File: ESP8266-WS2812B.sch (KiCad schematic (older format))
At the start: 17 parts, among them J1 USB_B_Micro, J2 Alternate_Power_Input, J3 Conn_01x06, J4 Conn_01x03, Q1 Q_NPN_BEC, SW1 SW_Push

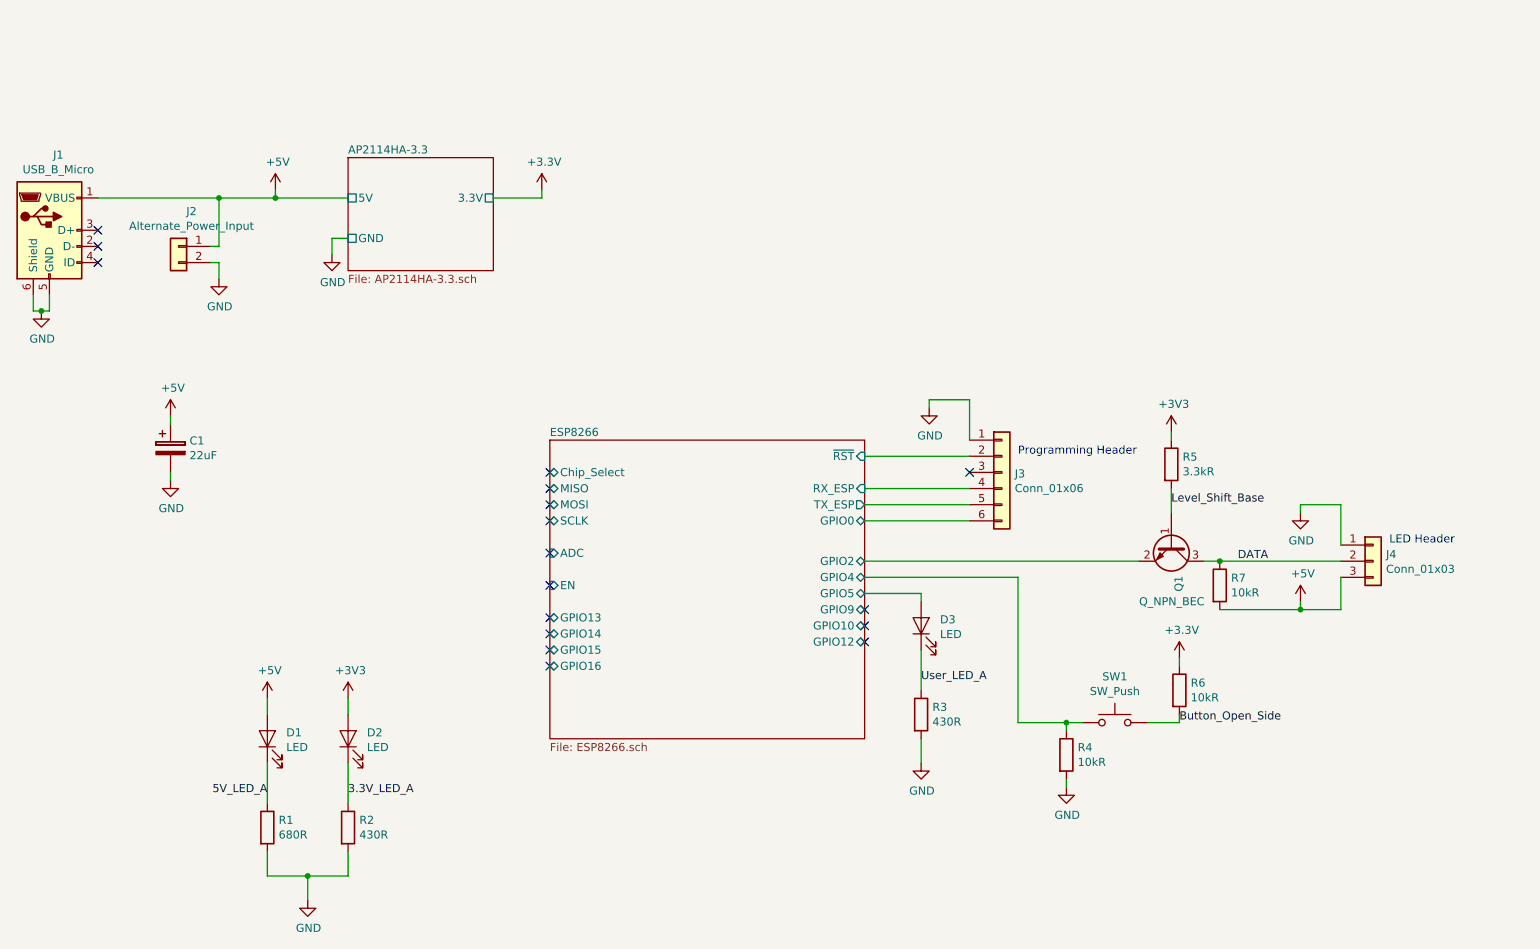
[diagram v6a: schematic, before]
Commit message: Generated netlist, added mounting holes and completed rough component placement on PCB.
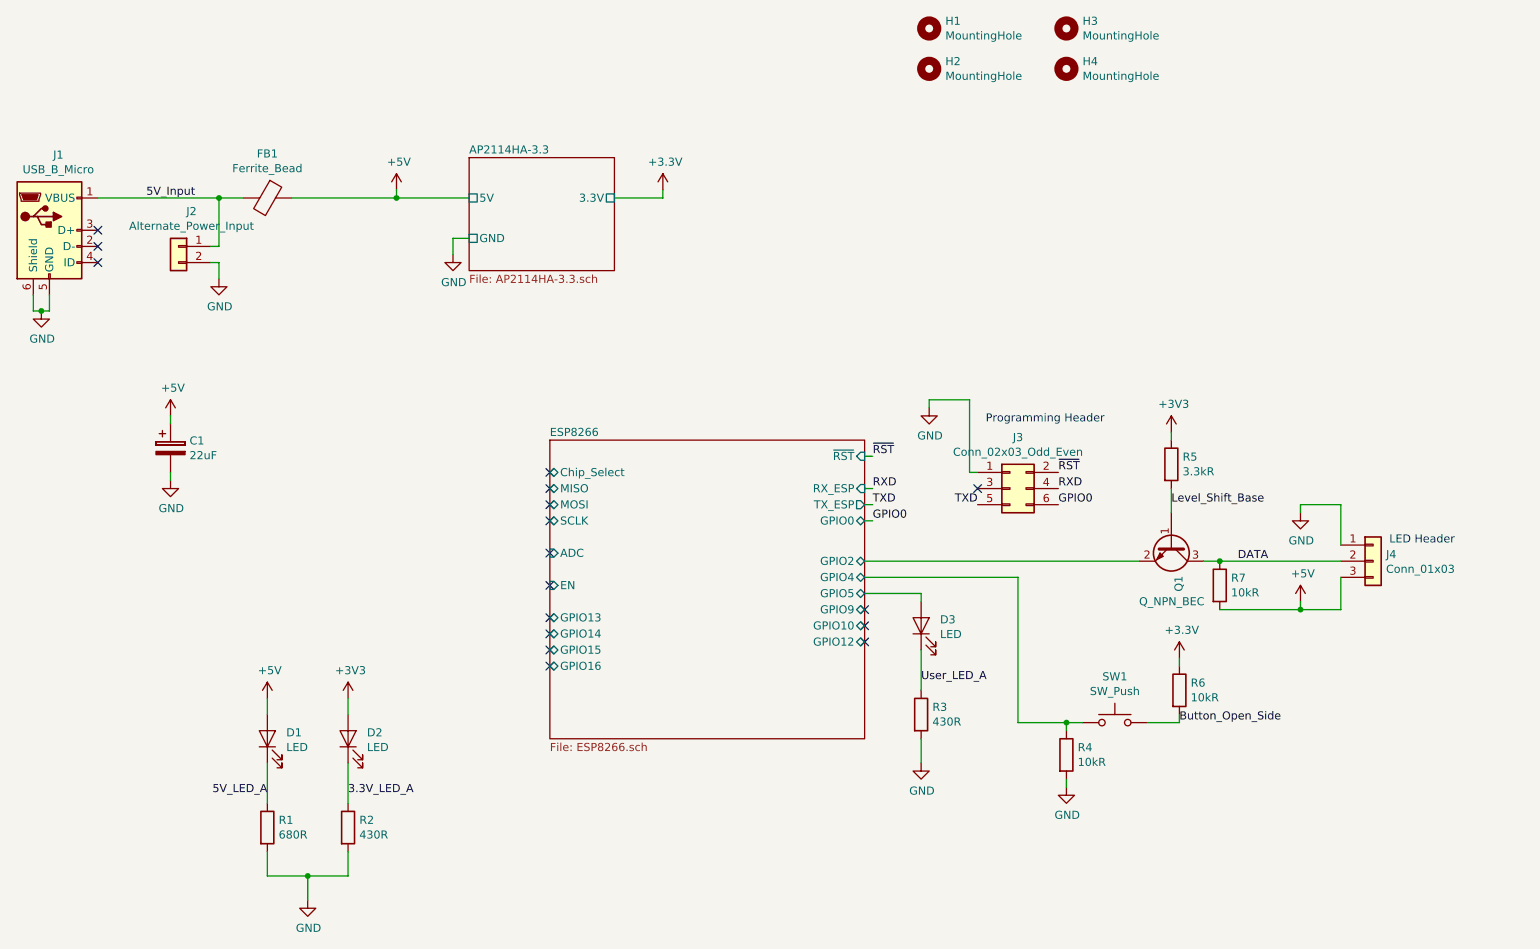
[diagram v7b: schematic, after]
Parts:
- removed J3: Conn_01x06, Pin_Headers:Pin_Header_Straight_1x06_Pitch2.54mm, symbol Connector_Generic:Conn_01x06
- added FB1: Ferrite_Bead, Inductors_SMD:L_0805, symbol Device:Ferrite_Bead
- added H1, H2, H3, H4: MountingHole, Mounting_Holes:MountingHole_2.5mm, symbol Mechanical:MountingHole
- added J3: Conn_02x03_Odd_Even, Pin_Headers:Pin_Header_Straight_2x03_Pitch2.54mm, symbol Connector_Generic:Conn_02x03_Odd_Even
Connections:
- net +5V: now also FB1.1; no longer J1.1 (VBUS), J2.1 (Pin_1)
- net GND: now also J3.1 (Pin_1)
- new net 5V_Input: FB1.2, J1.1 (VBUS), J2.1 (Pin_1)
- new net GPIO0: J3.6 (Pin_6)
- new net RXD: J3.4 (Pin_4)
- new net TXD: J3.5 (Pin_5)
- new net ~RST: J3.2 (Pin_2)
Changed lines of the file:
@@
 L power:+3.3V #PWR010
 U 1 1 5BC405C1
-P 4350 2450
-F 0 "#PWR010" H 4350 2300 50  0001 C CNN
-F 1 "+3.3V" H 4365 2623 50  0000 C CNN
-F 2 "" H 4350 2450 50  0001 C CNN
-F 3 "" H 4350 2450 50  0001 C CNN
-	1    4350 2450
-	1    0    0    -1
-$EndComp
-Wire Wire Line
-	4350 2450 4350 2500
+P 5100 2450
+F 0 "#PWR010" H 5100 2300 50  0001 C CNN
+F 1 "+3.3V" H 5115 2623 50  0000 C CNN
+F 2 "" H 5100 2450 50  0001 C CNN
+F 3 "" H 5100 2450 50  0001 C CNN
+	1    5100 2450
+	1    0    0    -1
+$EndComp
+Wire Wire Line
+	5100 2450 5100 2500
 $Comp
 L power:+5V #PWR06
 U 1 1 5BC40E42
-P 2700 2450
-F 0 "#PWR06" H 2700 2300 50  0001 C CNN
-F 1 "+5V" H 2715 2623 50  0000 C CNN
-F 2 "" H 2700 2450 50  0001 C CNN
-F 3 "" H 2700 2450 50  0001 C CNN
-	1    2700 2450
+P 3450 2450
+F 0 "#PWR06" H 3450 2300 50  0001 C CNN
+F 1 "+5V" H 3465 2623 50  0000 C CNN
+F 2 "" H 3450 2450 50  0001 C CNN
+F 3 "" H 3450 2450 50  0001 C CNN
+	1    3450 2450
 	1    0    0    -1
 $EndComp
@@
 $EndComp
 Wire Wire Line
-	2700 2450 2700 2500
+	3450 2450 3450 2500
 $Comp
 L power:GND #PWR01
@@
 NoConn ~ 1600 2800
 NoConn ~ 1600 2900
-$Comp
-L Connector_Generic:Conn_01x06 J3
-U 1 1 5BC50259
-P 7200 4200
-F 0 "J3" H 7280 4192 50  0000 L CNN
-F 1 "Conn_01x06" H 7280 4101 50  0000 L CNN
-F 2 "Pin_Headers:Pin_Header_Straight_1x06_Pitch2.54mm" H 7200 4200 50  0001 C CNN
-F 3 "~" H 7200 4200 50  0001 C CNN
-	1    7200 4200
-	1    0    0    -1
-$EndComp
-Text Notes 7300 4100 0    50   ~ 0
+Text Notes 7100 3900 0    50   ~ 0
 Programming Header
 $Comp
@@
 $EndComp
 Wire Wire Line
-	7000 4000 7000 3750
-Wire Wire Line
 	7000 3750 6750 3750
 Wire Wire Line
 	6750 3750 6750 3800
-NoConn ~ 7000 4200
 $Comp
 L power:GND #PWR016
@@
 F21 "GPIO0" T R 6350 4500 50
 $EndSheet
-Wire Wire Line
-	6350 4100 7000 4100
-Wire Wire Line
-	6350 4300 7000 4300
-Wire Wire Line
-	6350 4400 7000 4400
-Wire Wire Line
-	6350 4500 7000 4500
 NoConn ~ 4400 4700
 NoConn ~ 4400 4900
@@
 NoConn ~ 4400 4200
 $Sheet
-S 3150 2250 900  700
+S 3900 2250 900  700
 U 5BD89DA4
 F0 "AP2114HA-3.3" 50
 F1 "AP2114HA-3.3.sch" 50
-F2 "5V" U L 3150 2500 50
-F3 "3.3V" U R 4050 2500 50
-F4 "GND" U L 3150 2750 50
+F2 "5V" U L 3900 2500 50
+F3 "3.3V" U R 4800 2500 50
+F4 "GND" U L 3900 2750 50
 $EndSheet
 Wire Wire Line
-	4050 2500 4350 2500
-Wire Wire Line
-	3150 2750 3050 2750
-Wire Wire Line
-	3050 2750 3050 2850
+	4800 2500 5100 2500
+Wire Wire Line
+	3900 2750 3800 2750
+Wire Wire Line
+	3800 2750 3800 2850
 $Comp
 L power:GND #PWR08
 U 1 1 5BD8DB67
-P 3050 2850
-F 0 "#PWR08" H 3050 2600 50  0001 C CNN
-F 1 "GND" H 3055 2677 50  0000 C CNN
-F 2 "" H 3050 2850 50  0001 C CNN
-F 3 "" H 3050 2850 50  0001 C CNN
-	1    3050 2850
+P 3800 2850
+F 0 "#PWR08" H 3800 2600 50  0001 C CNN
+F 1 "GND" H 3805 2677 50  0000 C CNN
+F 2 "" H 3800 2850 50  0001 C CNN
+F 3 "" H 3800 2850 50  0001 C CNN
+	1    3800 2850
 	1    0    0    -1
 $EndComp
@@
 Wire Wire Line
 	1600 2500 2350 2500
-Connection ~ 2700 2500
-Wire Wire Line
-	2700 2500 3150 2500
+Connection ~ 3450 2500
+Wire Wire Line
+	3450 2500 3900 2500
 Wire Wire Line
 	2350 2800 2350 2500
-Connection ~ 2350 2500
-Wire Wire Line
-	2350 2500 2700 2500
 $Comp
 L power:GND #PWR04
@@
 Wire Wire Line
 	7300 4850 7300 5750
+$Comp
+L Device:Ferrite_Bead FB1
+U 1 1 5BE0F936
+P 2650 2500
+F 0 "FB1" V 2376 2500 50  0000 C CNN
+F 1 "Ferrite_Bead" V 2467 2500 50  0000 C CNN
+F 2 "Inductors_SMD:L_0805" V 2580 2500 50  0001 C CNN
+F 3 "~" H 2650 2500 50  0001 C CNN
+	1    2650 2500
+	0    1    1    0
+$EndComp
+Wire Wire Line
+	2350 2500 2500 2500
+Connection ~ 2350 2500
+Wire Wire Line
+	2800 2500 3450 2500
+Text Label 1900 2500 0    50   ~ 0
+5V_Input
+$Comp
+L Connector_Generic:Conn_02x03_Odd_Even J3
+U 1 1 5BE1A98A
+P 7250 4300
+F 0 "J3" H 7300 4617 50  0000 C CNN
+F 1 "Conn_02x03_Odd_Even" H 7300 4526 50  0000 C CNN
+F 2 "Pin_Headers:Pin_Header_Straight_2x03_Pitch2.54mm" H 7250 4300 50  0001 C CNN
+F 3 "~" H 7250 4300 50  0001 C CNN
+	1    7250 4300
+	1    0    0    -1
+$EndComp
+Text Label 6400 4100 0    50   ~ 0
+~RST
+Wire Wire Line
+	6350 4100 6400 4100
+Text Label 6400 4300 0    50   ~ 0
+RXD
+Wire Wire Line
+	6400 4300 6350 4300
+Text Label 6400 4400 0    50   ~ 0
+TXD
+Wire Wire Line
+	6400 4400 6350 4400
+Text Label 6400 4500 0    50   ~ 0
+GPIO0
+Wire Wire Line
+	6400 4500 6350 4500
+Wire Wire Line
+	7000 4200 7050 4200
+Wire Wire Line
+	7000 3750 7000 4200
+NoConn ~ 7050 4300
+Text Label 7550 4200 0    50   ~ 0
+~RST
+Text Label 7550 4300 0    50   ~ 0
+RXD
+Text Label 7050 4400 2    50   ~ 0
+TXD
+Text Label 7550 4400 0    50   ~ 0
+GPIO0
+$Comp
+L Mechanical:MountingHole H1
+U 1 1 5BE26377
+P 6750 1450
+F 0 "H1" H 6850 1496 50  0000 L CNN
+F 1 "MountingHole" H 6850 1405 50  0000 L CNN
+F 2 "Mounting_Holes:MountingHole_2.5mm" H 6750 1450 50  0001 C CNN
+F 3 "~" H 6750 1450 50  0001 C CNN
+	1    6750 1450
+	1    0    0    -1
+$EndComp
+$Comp
+L Mechanical:MountingHole H3
+U 1 1 5BE2687A
+P 7600 1450
+F 0 "H3" H 7700 1496 50  0000 L CNN
+F 1 "MountingHole" H 7700 1405 50  0000 L CNN
+F 2 "Mounting_Holes:MountingHole_2.5mm" H 7600 1450 50  0001 C CNN
+F 3 "~" H 7600 1450 50  0001 C CNN
+	1    7600 1450
+	1    0    0    -1
+$EndComp
+$Comp
+L Mechanical:MountingHole H2
+U 1 1 5BE268DA
+P 6750 1700
+F 0 "H2" H 6850 1746 50  0000 L CNN
+F 1 "MountingHole" H 6850 1655 50  0000 L CNN
+F 2 "Mounting_Holes:MountingHole_2.5mm" H 6750 1700 50  0001 C CNN
+F 3 "~" H 6750 1700 50  0001 C CNN
+	1    6750 1700
+	1    0    0    -1
+$EndComp
+$Comp
+L Mechanical:MountingHole H4
+U 1 1 5BE26922
+P 7600 1700
+F 0 "H4" H 7700 1746 50  0000 L CNN
+F 1 "MountingHole" H 7700 1655 50  0000 L CNN
+F 2 "Mounting_Holes:MountingHole_2.5mm" H 7600 1700 50  0001 C CNN
+F 3 "~" H 7600 1700 50  0001 C CNN
+	1    7600 1700
+	1    0    0    -1
+$EndComp
 $EndSCHEMATC
